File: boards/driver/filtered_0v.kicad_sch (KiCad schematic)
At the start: 3 parts

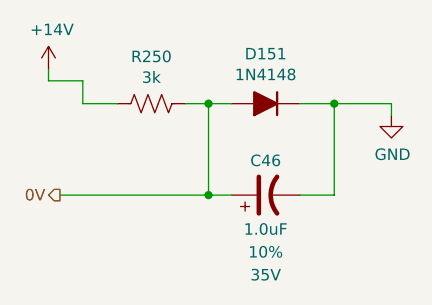
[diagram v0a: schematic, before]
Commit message: Driver: Added a 5V->3.3V LDO to replace the reversed cmod header, added jumpers for the 200R parallel returns, and renamed subcircuit ports to avoid unexpected ground connections.
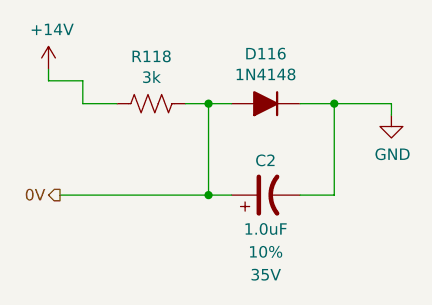
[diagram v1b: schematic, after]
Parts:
- renumbered C46 to C2, D151 to D116, R250 to R118
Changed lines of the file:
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@@
   (symbol (lib_id "Device:C_Polarized_US") (at 129.54 101.6 90)
     (in_bom yes) (on_board yes)
-    (property "Reference" "C46" (id 0) (at 129.54 97.79 90))
+    (property "Reference" "C2" (id 0) (at 129.54 97.79 90))
     (property "Value" "1.0uF" (id 1) (at 129.54 105.41 90))
     (property "Footprint" "Capacitor_Tantalum_SMD:CP_EIA-3528-21_Kemet-B" (id 2) (at 129.54 101.6 0)
@@
   (symbol (lib_id "lachesis:+14V") (at 105.41 87.63 0)
     (in_bom yes) (on_board yes)
-    (property "Reference" "#PWR0123" (id 0) (at 105.41 91.44 0)
+    (property "Reference" "#PWR025" (id 0) (at 105.41 91.44 0)
       (effects (font (size 1.27 1.27)) hide)
     )
@@
   (symbol (lib_id "Device:R_US") (at 116.84 91.44 270)
     (in_bom yes) (on_board yes)
-    (property "Reference" "R250" (id 0) (at 116.84 86.233 90))
+    (property "Reference" "R118" (id 0) (at 116.84 86.233 90))
     (property "Value" "3k" (id 1) (at 116.84 88.5444 90))
     (property "Footprint" "Resistor_SMD:R_0603_1608Metric" (id 2) (at 116.586 92.456 90)
@@
   (symbol (lib_id "Device:D_Filled") (at 129.54 91.44 180)
     (in_bom yes) (on_board yes)
-    (property "Reference" "D151" (id 0) (at 129.54 85.9282 0))
+    (property "Reference" "D116" (id 0) (at 129.54 85.9282 0))
     (property "Value" "1N4148" (id 1) (at 129.54 88.2396 0))
     (property "Footprint" "Diode_SMD:D_SOD-323" (id 2) (at 129.54 91.44 0)
@@
   (symbol (lib_id "power:GND") (at 143.51 92.71 0)
     (in_bom yes) (on_board yes)
-    (property "Reference" "#PWR0124" (id 0) (at 143.51 99.06 0)
+    (property "Reference" "#PWR026" (id 0) (at 143.51 99.06 0)
       (effects (font (size 1.27 1.27)) hide)
     )

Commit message: Driver: incorporated most changes from the test board, and began layout
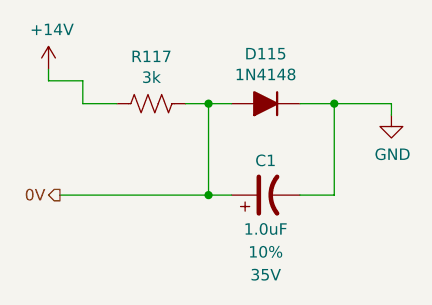
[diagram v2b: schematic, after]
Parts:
- D115: renamed from D116; footprint Diode_SMD:D_SOD-323 -> lachesis:D_SOD-323
- renumbered C2 to C1, R118 to R117
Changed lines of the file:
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@@
     (effects (font (size 1.27 1.27)) (justify right))
   )
-  (symbol (lib_id "Device:C_Polarized_US") (at 129.54 101.6 90)
+  (symbol (lib_id "Device:C_Polarized_US") (at 129.54 101.6 90) (unit 1)
     (in_bom yes) (on_board yes)
-    (property "Reference" "C2" (id 0) (at 129.54 97.79 90))
+    (property "Reference" "C1" (id 0) (at 129.54 97.79 90))
     (property "Value" "1.0uF" (id 1) (at 129.54 105.41 90))
     (property "Footprint" "Capacitor_Tantalum_SMD:CP_EIA-3528-21_Kemet-B" (id 2) (at 129.54 101.6 0)
@@
     (pin "2")
   )
-  (symbol (lib_id "lachesis:+14V") (at 105.41 87.63 0)
+  (symbol (lib_id "lachesis:+14V") (at 105.41 87.63 0) (unit 1)
     (in_bom yes) (on_board yes)
-    (property "Reference" "#PWR025" (id 0) (at 105.41 91.44 0)
+    (property "Reference" "#PWR023" (id 0) (at 105.41 91.44 0)
       (effects (font (size 1.27 1.27)) hide)
     )
@@
     (pin "1")
   )
-  (symbol (lib_id "Device:R_US") (at 116.84 91.44 270)
+  (symbol (lib_id "Device:R_US") (at 116.84 91.44 270) (unit 1)
     (in_bom yes) (on_board yes)
-    (property "Reference" "R118" (id 0) (at 116.84 86.233 90))
+    (property "Reference" "R117" (id 0) (at 116.84 86.233 90))
     (property "Value" "3k" (id 1) (at 116.84 88.5444 90))
     (property "Footprint" "Resistor_SMD:R_0603_1608Metric" (id 2) (at 116.586 92.456 90)
@@
     (pin "2")
   )
-  (symbol (lib_id "Device:D_Filled") (at 129.54 91.44 180)
+  (symbol (lib_id "Device:D_Filled") (at 129.54 91.44 180) (unit 1)
     (in_bom yes) (on_board yes)
-    (property "Reference" "D116" (id 0) (at 129.54 85.9282 0))
+    (property "Reference" "D115" (id 0) (at 129.54 85.9282 0))
     (property "Value" "1N4148" (id 1) (at 129.54 88.2396 0))
-    (property "Footprint" "Diode_SMD:D_SOD-323" (id 2) (at 129.54 91.44 0)
+    (property "Footprint" "lachesis:D_SOD-323" (id 2) (at 129.54 91.44 0)
       (effects (font (size 1.27 1.27)) hide)
     )
@@
     (pin "2")
   )
-  (symbol (lib_id "power:GND") (at 143.51 92.71 0)
+  (symbol (lib_id "power:GND") (at 143.51 92.71 0) (unit 1)
     (in_bom yes) (on_board yes)
-    (property "Reference" "#PWR026" (id 0) (at 143.51 99.06 0)
+    (property "Reference" "#PWR024" (id 0) (at 143.51 99.06 0)
       (effects (font (size 1.27 1.27)) hide)
     )

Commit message: Driver: minor schematic cleanup and populated all of the BOM except for resistors
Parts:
- C1: MPN (none) -> T495B105K035ATE1K5; Manufacturer (none) -> KEMET; Package (none) -> 1411
- D115: MPN (none) -> 1N4148WS; Manufacturer (none) -> SMC Diode Solutions; Package (none) -> SOD-323; Rating (none) -> 300mA
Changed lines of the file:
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@@
+      (effects (font (size 1.27 1.27)) hide)
+    )
+    (property "Description" "CAP TANT 1UF 10% 35V 1411" (id 9) (at 129.54 101.6 0)
+      (effects (font (size 1.27 1.27)) hide)
+    )
+    (property "MPN" "T495B105K035ATE1K5" (id 10) (at 129.54 101.6 0)
+      (effects (font (size 1.27 1.27)) hide)
+    )
+    (property "Manufacturer" "KEMET" (id 11) (at 129.54 101.6 0)
+      (effects (font (size 1.27 1.27)) hide)
+    )
+    (property "Package" "1411" (id 12) (at 129.54 101.6 0)
       (effects (font (size 1.27 1.27)) hide)
     )
@@
       (effects (font (size 1.27 1.27)) hide)
     )
+    (property "MPN" "1N4148WS" (id 6) (at 129.54 91.44 0)
+      (effects (font (size 1.27 1.27)) hide)
+    )
+    (property "Manufacturer" "SMC Diode Solutions" (id 7) (at 129.54 91.44 0)
+      (effects (font (size 1.27 1.27)) hide)
+    )
+    (property "Description" "DIODE GEN PURP 75V 300MA SOD323" (id 8) (at 129.54 91.44 0)
+      (effects (font (size 1.27 1.27)) hide)
+    )
+    (property "Package" "SOD-323" (id 9) (at 129.54 91.44 0)
+      (effects (font (size 1.27 1.27)) hide)
+    )
+    (property "Rating" "300mA" (id 10) (at 129.54 91.44 0)
+      (effects (font (size 1.27 1.27)) hide)
+    )

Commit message: Driver: filled out the rest of the BOM, except for defaults for nominal resistances
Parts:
- R117: MPN (none) -> ERJ-PA3F3001V; Manufacturer (none) -> Panasonic Electronic Components; Package (none) -> 0603; Rating 1/4W -> 1/3W
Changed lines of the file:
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@@
       (effects (font (size 1.27 1.27)) hide)
     )
-    (property "Rating" "1/4W" (id 5) (at 116.84 91.44 90)
+    (property "Rating" "1/3W" (id 5) (at 116.84 91.44 90)
       (effects (font (size 1.27 1.27)) hide)
     )
@@
       (effects (font (size 1.27 1.27)) hide)
     )
+    (property "Description" "RES SMD 3K OHM PULSE-WITHSTANDING 1% 1/3W 0603" (id 8) (at 116.84 91.44 0)
+      (effects (font (size 1.27 1.27)) hide)
+    )
+    (property "MPN" "ERJ-PA3F3001V" (id 9) (at 116.84 91.44 0)
+      (effects (font (size 1.27 1.27)) hide)
+    )
+    (property "Manufacturer" "Panasonic Electronic Components" (id 10) (at 116.84 91.44 0)
+      (effects (font (size 1.27 1.27)) hide)
+    )
+    (property "Package" "0603" (id 11) (at 116.84 91.44 0)
+      (effects (font (size 1.27 1.27)) hide)
+    )
